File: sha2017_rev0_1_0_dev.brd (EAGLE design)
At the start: 95 x 86 mm, 184 parts, among them IC1 AP7215, IC2 CPT112, IC3 CP210X_USB_UART, IC4 ESP32WROOM32, IC5 MCP73833, IC6 FXL6408, Q1 MMBT2222A, Q2 MMBT2222A, Q3 SI1304 BDL, Q4 MOSFET-PCHANNEL, Q5 MMBT2222A, Q6 MOSFET-PCHANNEL, Q7 MMBT2222A, Q8 MMBT2222A, T1 SI2301DS, X1_ JST-PH3, X701 2908-05WB-MG

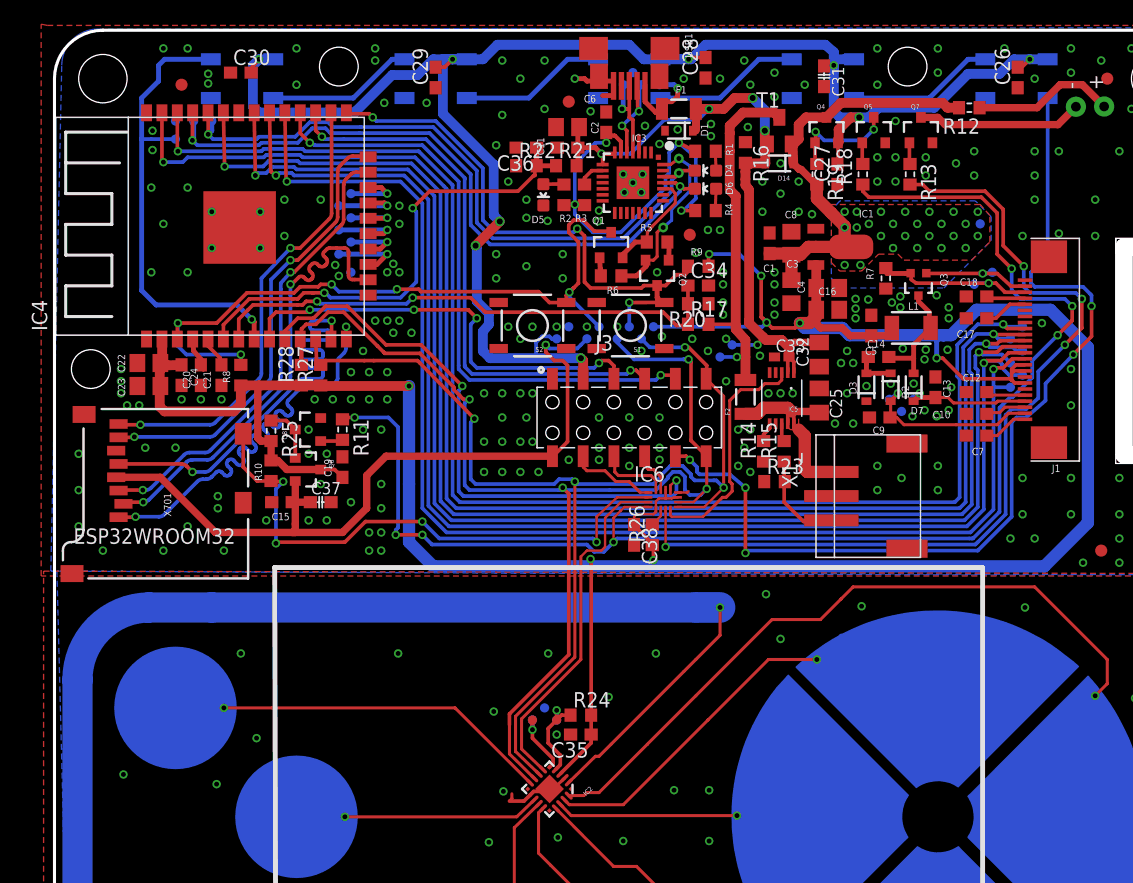
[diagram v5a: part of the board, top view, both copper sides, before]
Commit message: renumbered PCB and placed designators
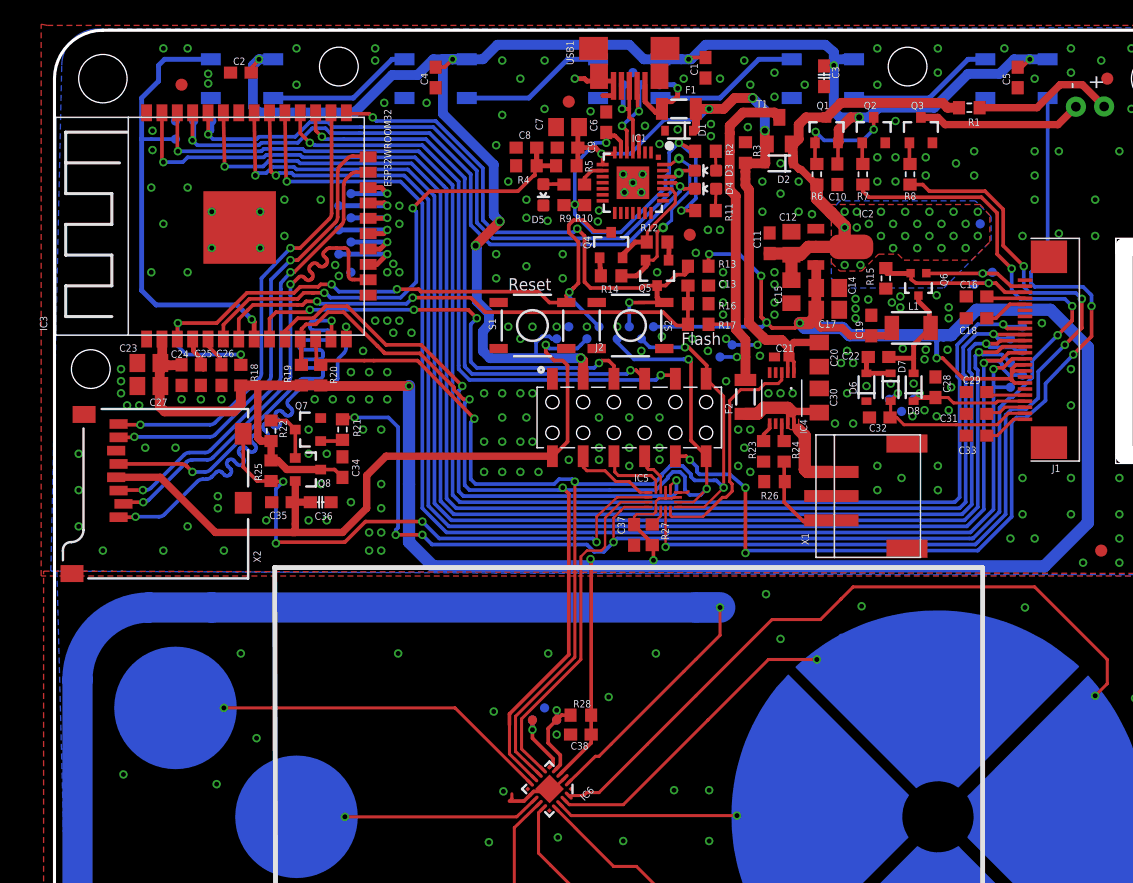
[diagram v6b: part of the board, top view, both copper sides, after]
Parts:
- removed D14: NSVR0320MW2T1G, SparkFun-DiscreteSemi:SOD-323
- removed U$29, U$30: VIA, badge:VIA
- added $$U$7, $$U$9: VIA, badge:VIA
- added D8: NSVR0320MW2T1G, SparkFun-DiscreteSemi:SOD-323
- C10, C13, C19, C9: value 1u -> 100n
- C12, C14, C17, C7: value 1u -> 4u7/16V; device rcl:C0603 -> rcl:C0805
- C15, C27: value 100n -> 4u7/16V; device rcl:C0603 -> rcl:C0805
- C16, C22: value 4u7/16V -> 1u; device rcl:C0805 -> rcl:C0603
- C2, C4, C8: value 4u7/16V -> 100n; device rcl:C0805 -> rcl:C0603
- C20: value (none) -> 10uF; device rcl:C0603 -> rcl:C0805K
- C21: value (none) -> 100nF; device rcl:C0603 -> rcl:C0402K
- C25: value 10uF -> (none); device rcl:C0805K -> rcl:C0603
- C26: value 100n -> (none)
- C28, C29, C34: value 100n -> 1u
- C3: device rcl:C0805 -> 00ralf:C0603-DASHES
- C30: value 100n -> 10uF; device rcl:C0603 -> rcl:C0805K
- C31: value 4u7/16V -> 1u; device 00ralf:C0603-DASHES -> rcl:C0603
- C32: value 10uF -> 1u; device rcl:C0805K -> rcl:C0603
- C33: value 100nF -> 1u; device rcl:C0402K -> rcl:C0603
- C36: value 100n -> 4u7/16V; device rcl:C0603 -> 00ralf:C0603-DASHES
- C37: value 4u7/16V -> (none); device 00ralf:C0603-DASHES -> rcl:C0603
- C38: value (none) -> 100n
- D3: value NSVR0320MW2T1G -> Yellow; device SparkFun-DiscreteSemi:SOD-323 -> SparkFun-LED:LED-0603
- D4: value Yellow -> RED
- D6: value RED -> NSVR0320MW2T1G; device SparkFun-LED:LED-0603 -> SparkFun-DiscreteSemi:SOD-323
- IC1: value AP7215 -> CP210X_USB_UART; device badge:SOT89 -> SparkFun-DigitalIC:MLP28
- IC2: value CPT112 -> AP7215; device badge:QFN20-3X3MM -> badge:SOT89
- IC3: value CP210X_USB_UART -> ESP32WROOM32; device SparkFun-DigitalIC:MLP28 -> ESP3x:ESP32MOD
- IC4: value ESP32WROOM32 -> MCP73833; device ESP3x:ESP32MOD -> SparkFun:MSOP-10
- IC5: value MCP73833 -> FXL6408; device SparkFun:MSOP-10 -> badge:UMLP-16
- IC6: value FXL6408 -> CPT112; device badge:UMLP-16 -> badge:QFN20-3X3MM
- Q1, Q8: value MMBT2222A -> MOSFET-PCHANNEL
- Q3: value SI1304 BDL -> MMBT2222A; device SparkFun-DiscreteSemi:SOT323 -> SparkFun-DiscreteSemi:SOT23-3
- Q4: value MOSFET-PCHANNEL -> MMBT2222A
- Q6: value MOSFET-PCHANNEL -> SI1304 BDL; device SparkFun-DiscreteSemi:SOT23-3 -> SparkFun-DiscreteSemi:SOT323
- R1: value 1k -> 10R; device rcl:R0603 -> 00ralf:R0603-DASHES
- R10: value 100k -> 10k
- R11: value 10k -> 1k; device 00ralf:R0603-DASHES -> rcl:R0603
- R12: value 10R -> 10k; device 00ralf:R0603-DASHES -> rcl:R0603
- R13, R18: device 00ralf:R0603-DASHES -> rcl:R0603
- R14: value 2.2k -> 10k
- R15: value 1k -> 5R; device rcl:R0603 -> 00ralf:R0603-DASHES
- R16: value 10k -> 100k
- R19: value 10k -> 470R; device 00ralf:R0603-DASHES -> rcl:R0603
- R20: value 100k -> 470R
- R21: value 220k -> 10k; device rcl:R0603 -> 00ralf:R0603-DASHES
- R22: value 100k -> 10k; device rcl:R0603 -> 00ralf:R0603-DASHES
- R23: value 150k -> 2.2k
- R25: value 10k -> 100k; device 00ralf:R0603-DASHES -> rcl:R0603
- R26: value 10k -> 150k
- R27: value 470R -> 10k
- R28: value 470R -> 1k
- R4: value 1k -> 100k
- R5: value 10k -> 220k
- R6, R8: device rcl:R0603 -> 00ralf:R0603-DASHES
- R7: value 5R -> 10k
- R9: value 10k -> 1k
- moved FD1 76.5 mm to (87.0, 81.0)
- moved FD2 76.5 mm to (10.5, 80.5)
- moved U$23 73.6 mm to (87.6, 6.70)
- moved C26 70.2 mm to (13.8, 56.5)
- moved U$2 60.8 mm to (58.8, 38.4)
- moved C22 60.3 mm to (68.1, 58.0), turned to 0 degrees
- moved C27 59.5 mm to (7.80, 55.6), turned to 180 degrees
- moved R8 57.7 mm to (70.7, 73.1), turned to 270 degrees
- moved Q7 56.3 mm to (21.0, 52.0), turned to 90 degrees
- moved C30 54.9 mm to (63.2, 54.4), turned to 270 degrees
- moved R18 54.0 mm to (15.4, 56.5)
- moved Q6 52.8 mm to (71.4, 64.0), turned to 180 degrees
- moved U$11 52.3 mm to (5.70, 23.5)
- moved U$21 52.3 mm to (56.4, 10.7)
- moved U$20 52.0 mm to (35.9, 11.9)
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- renumbered D10 to D101, D11 to D102, D12 to D103, D13 to D104, D9 to D100, J3 to J2, TB1 to TB104, TB2 to TB103, TB3 to TB101, TB4 to TB100, TB5 to TB102, TP10 to TP107, TP11 to TP106, TP12 to TP104, TP13 to TP105, TP14 to TP131, TP15 to TP130, TP16 to TP129, TP17 to TP127, TP18 to TP126, TP19 to TP125, TP20 to TP113, TP22 to TP114, TP23 to TP119, TP24 to TP120, TP25 to TP116, TP26 to TP115, TP27 to TP109, TP28 to TP118, TP29 to TP128, TP3 to TP100, TP30 to TP111, TP31 to TP132, TP32 to TP121, TP33 to TP133, TP34 to TP134, TP35 to TP137, TP36 to TP138, TP37 to TP108, TP38 to TP103, TP39 to TP124, TP4 to TP101, TP40 to TP135, TP41 to TP139, TP42 to TP102, TP43 to TP136, TP5 to TP123, TP6 to TP122, TP7 to TP117, TP8 to TP112, TP9 to TP110, U$31 to $$U$8, X1_ to X1, X701 to X2
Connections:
- net +3V3: now also C14.1, C17.1, C27.1, C34.1, C37.1, IC2.3, IC3.2, IC5.15, IC5.2, IC5.9, IC6.4, Q8.3, R13.2, R18.1, R19.1, R20.1, R22.2, R25.1, R28.2; no longer C16.1, C22.1, C35.1, C4.1, C5.1, IC1.3, IC2.4, IC4.2, IC6.15, IC6.2, IC6.9, Q6.3, R10.1, R24.2, R25.2, R26.1, R28.1, R8.1, R9.2
- net +5V: now also C20.2, C21.2, C7.1, C9.1, D2.A, IC1.7, IC1.8, IC4.1, IC4.2, R3.2, R5.2; no longer C11.1, C2.1, C32.2, C33.2, D14.A, IC3.7, IC3.8, IC5.1, IC5.2, R16.2, R21.2
- net 3V3_SWITCHED: now also C35.1, C36.1, Q8.2; no longer C15.1, C37.1, Q6.2
- net CHRG_STAT: now also IC4.3, IC5.12; no longer IC5.3, IC6.12
- net ESP32_!RESET: now also IC3.3, Q4.3, R18.2, S1.3; no longer IC4.3, Q1.3, R8.2, S2.3
- net ESP32_FLASH: now also IC3.25, Q5.3, R13.1, S2.3; no longer IC4.25, Q2.3, R9.1, S1.3
- net ESP32_RX: now also D3.C, IC1.26, IC3.34; no longer D4.C, IC3.26, IC4.34
- net ESP32_TX: now also D4.C, IC1.25, IC3.35; no longer D6.C, IC3.25, IC4.35
- net EXTIO-0: now also IC3.9; no longer IC4.9
- net EXTIO-1: now also IC3.27; no longer IC4.27
- net EXTIO-2: now also IC3.28; no longer IC4.28
- net EXTIO-3: now also IC5.3; no longer IC6.3
- net EXTIO-4: now also IC5.4; no longer IC6.4
- net EXTIO-5: now also IC5.5; no longer IC6.5
- net GDR: now also Q6.1; no longer Q3.1
- net GND: now also $$U$7.P$1, $$U$9.P$1, C1.1, C12.2, C13.2, C14.2, C16.1, C17.2, C2.1, C27.2, C31.1, C4.1, C5.1, C7.2, C9.2, D6.C, IC1.3, IC1.EXP, IC1.M, IC2.1, IC3.0, IC3.1, IC3.15, IC3.38, IC4.5, IC5.16, IC6.12, IC6.3, Q2.2, Q3.2, R15.2, R26.1, R3.1, R4.1; no longer C1.2, C12.1, C13.1, C16.2, C17.1, C2.2, C22.2, C27.1, C31.2, C4.2, C5.2, C7.1, C9.1, D3.C, IC1.1, IC2.12, IC2.3, IC3.3, IC3.EXP, IC3.M, IC4.0, IC4.1, IC4.15, IC4.38, IC5.5, IC6.16, Q5.2, Q8.2, R14.1, R20.1, R22.1, R7.2, U$29.P$1, U$30.P$1
- net I2C_INT: now also IC3.10, IC5.1; no longer IC4.10, IC6.1
- net I2C_SCL: now also IC3.12, IC5.13, IC6.8, R20.2; no longer IC2.8, IC4.12, IC6.13, R27.2
- net I2C_SDA: now also IC3.11, IC5.14, IC6.9, R19.2; no longer IC2.9, IC4.11, IC6.14, R28.2
- net LCD_!RESET: now also IC3.37; no longer IC4.37
- net LCD_BUSY: now also IC3.36; no longer IC4.36
- net LCD_CS: now also IC3.31; no longer IC4.31
- net LCD_D/!S: now also IC3.33; no longer IC4.33
- net LCD_MOSI: now also IC3.29; no longer IC4.29
- net LCD_SCK: now also IC3.30; no longer IC4.30
- net N$1: now also IC6.10; no longer IC2.10
- net N$10: now also IC1.24, Q4.2, R12.1; no longer IC3.24, Q1.2, R5.1
- net N$11: now also IC1.28, Q5.2, R14.1; no longer IC3.28, Q2.2, R6.1
- net N$12: now also IC3.22; no longer IC4.22
- net N$13: now also Q5.1, R12.2; no longer Q2.1, R5.2
- net N$14: now also Q4.1, R14.2; no longer Q1.1, R6.2
- net N$15: now also Q7.1, R21.2; no longer Q8.1, R11.2
- net N$16: now also Q3.3; no longer Q7.3
- net N$17: now also Q7.3, Q8.1, R22.1; no longer Q6.1, Q8.3, R25.1
- net N$18: now also R1.1; no longer R12.1
- net N$22: now also C22.1, D6.A, D7.C; no longer C14.1, D2.C, D3.A
- net N$23: now also C22.2, D8.A, Q6.3; no longer C14.2, D7.A, Q3.3
- net N$25: now also IC6.20; no longer IC2.20
- net N$26: now also R9.1; no longer R2.1
- net N$27: now also D3.A, R2.1; no longer D4.A, R1.1
- net N$28: now also D4.A, R11.1; no longer D6.A, R4.1
- net N$3: now also IC3.17; no longer IC4.17
- net N$4: now also IC3.18; no longer IC4.18
- net N$42: now also C25.2, IC3.4; no longer C20.2, IC4.4
- net N$43: now also C26.2, IC3.5; no longer C21.2, IC4.5
- net N$45: now also Q3.1, R8.1; no longer Q7.1, R13.1
- net N$46: now also IC4.6, R23.2; no longer IC5.6, R14.2
- net N$47: now also IC4.8, R24.2; no longer IC5.8, R15.2
- net N$48: now also R24.1, R26.2; no longer R15.1, R23.2
- net N$49: now also C30.2, IC4.10, IC4.9; no longer C25.2, IC5.10, IC5.9
- net N$52: now also Q2.1, R7.2; no longer Q5.1, R18.2
- net N$53: now also Q1.1, Q2.3, R6.1; no longer Q4.1, Q5.3, R19.1
- net N$55: now also IC6.19; no longer IC2.19
- net N$56: now also IC6.18; no longer IC2.18
- net N$57: now also IC6.17; no longer IC2.17
- net N$58: now also IC6.13; no longer IC2.13
- net N$59: now also IC5.10, R27.2; no longer IC6.10, R26.2
- net N$6: now also IC3.19; no longer IC4.19
- net N$61: now also IC6.5, R28.1, TP2.P$1; no longer IC2.5, R24.1, TP1.P$1
- net N$62: now also IC6.6, TP1.P$1; no longer IC2.6, TP2.P$1
- net N$64: now also IC6.14; no longer IC2.14
- net N$65: now also IC6.15; no longer IC2.15
- net N$7: now also IC3.20; no longer IC4.20
- net N$8: now also IC1.9, R10.2; no longer IC3.9, R3.2
- net N$9: now also IC3.21; no longer IC4.21
- net PREVGH: now also C28.2, D8.C; no longer C13.2, D7.C
- net PREVGL: now also C32.2, D7.A; no longer C9.2, D2.A
- net PROXIMITY: now also IC6.2; no longer IC2.2
- net RESE: now also Q6.2, R15.1; no longer Q3.2, R7.1
- net SD_CD: now also IC5.6, R25.2; no longer IC6.6, R10.2
- net SD_CLK: now also IC3.13; no longer IC4.13
- net SD_CMD: now also IC3.23; no longer IC4.23
- net SD_DATA0: now also IC3.24; no longer IC4.24
- net SD_DATA1: now also IC3.26; no longer IC4.26
- net SD_DATA2: now also IC3.14; no longer IC4.14
- net SD_DATA3: now also IC3.16; no longer IC4.16
- net TOUCH_INT: now also IC5.7; no longer IC2.7
- net USB_DN_CON: now also IC1.5; no longer IC3.5
- net USB_DP_CON: now also IC1.4; no longer IC3.4
- net VBAT_SENSE: now also C13.1, IC3.7, R16.2; no longer C34.1, IC4.7, R20.2
- net VCC: now also C11.1, C12.1, C15.1, D2.C, IC2.2, IC2.2@, Q1.3, R1.2, R6.2; no longer C1.1, C3.1, C8.1, D14.C, IC1.2, IC1.2@, Q4.3, R12.2, R19.2
- net VCOM: now also C33.2; no longer C7.2
- net VDD: now also IC1.6, R10.1, R11.2, R9.2; no longer IC3.6, R1.2, R3.1, R4.2
- net VGH: now also C18.2; no longer C17.2
- net VGL: now also C16.2; no longer C18.2
- net VIBRATOR: now also IC5.11, R8.2; no longer IC6.11, R13.2
- net VSH: now also C29.2; no longer C12.2
- net VSL: now also C31.2; no longer C10.2
- net VUSB_SENSE: now also C8.1, IC3.6, R4.2, R5.1; no longer C36.1, IC4.6, R21.1, R22.2
- net WS2812_DATA: now also IC3.8; no longer IC4.8
- net WS2812_POWER: now also C1.2, C10.2, C2.2, C3.1, C4.2, C5.2, Q1.2; no longer C26.2, C27.2, C28.2, C29.2, C30.2, C31.1, Q4.2
- net WS2812_POWER_EN: now also IC5.8, R21.1, R7.1; no longer IC6.8, R11.1, R18.1
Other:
- board text added: "Flash"
- board text added: "Reset"

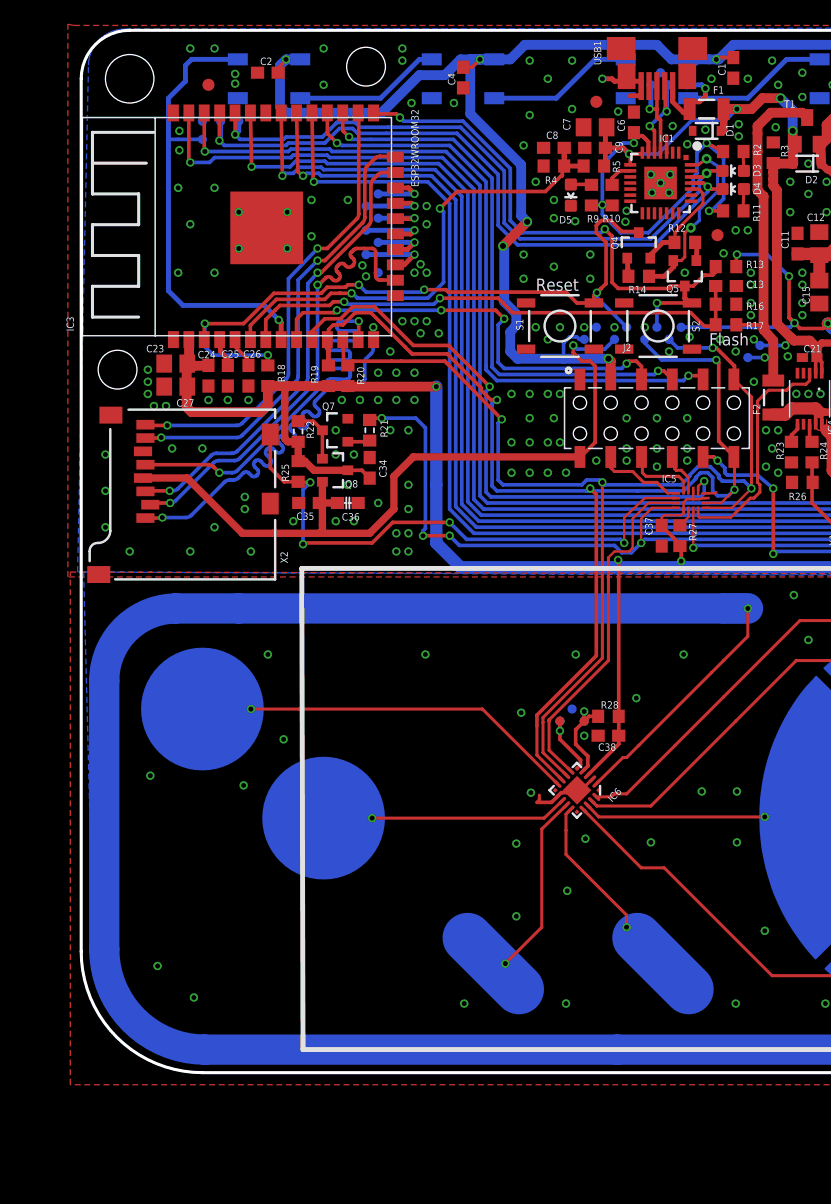
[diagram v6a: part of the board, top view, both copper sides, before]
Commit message: added SDIO pullups and some bootstrap magic for it
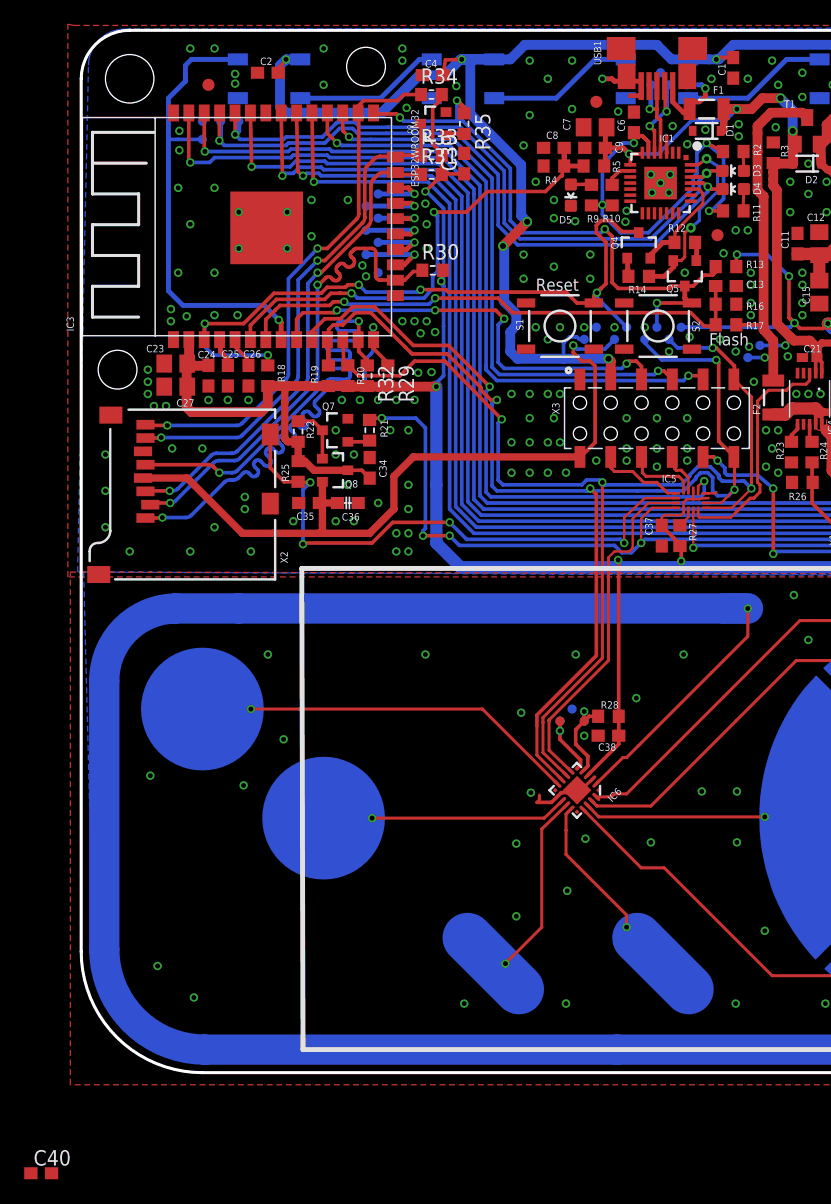
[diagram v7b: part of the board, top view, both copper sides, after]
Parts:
- added C39, C40: 100n, rcl:C0603
- added Q9: MMBT2222A, SparkFun-DiscreteSemi:SOT23-3
- added R29, R30, R31, R32, R33, R34, R35: 10k, 00ralf:R0603-DASHES
- moved C4 2.51 mm to (29.0, 81.3), turned to 0 degrees
- renumbered J2 to X3
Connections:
- new net N$20: Q9.1, R35.2
- net +3V3: now also C39.1, C40.1, R29.2, R30.2, R31.2, R32.2, R33.2, R34.2
- net ESP32_FLASH: now also R35.1
- net GND: now also C39.2, C40.2, Q9.2
- net SD_CLK: now also R32.1
- net SD_CMD: now also R31.1
- net SD_DATA0: now also Q9.3, R33.1
- net SD_DATA1: now also R34.1
- net SD_DATA2: now also R29.1
- net SD_DATA3: now also R30.1
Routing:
- net +3V3: track 238.6 -> 269.3 mm, vias 8 -> 10
- net SD_DATA1: track 38.0 -> 44.2 mm
- net WS2812_POWER: track 142.0 -> 147.3 mm
- net SD_DATA0: track 37.4 -> 42.2 mm
- net ESP32_FLASH: track 47.4 -> 50.4 mm, vias 3 -> 4
- net SD_DATA2: track 35.8 -> 38.5 mm
- net SD_DATA3: track 37.6 -> 40.2 mm
- net SD_CLK: track 37.3 -> 39.8 mm
- net SD_CMD: track 37.9 -> 40.1 mm
- net N$20: track 0.00 -> 1.54 mm
- net I2C_SCL: track 93.9 -> 95.3 mm
- net GND: vias 275 -> 276
